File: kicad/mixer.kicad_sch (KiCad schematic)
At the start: 1 part

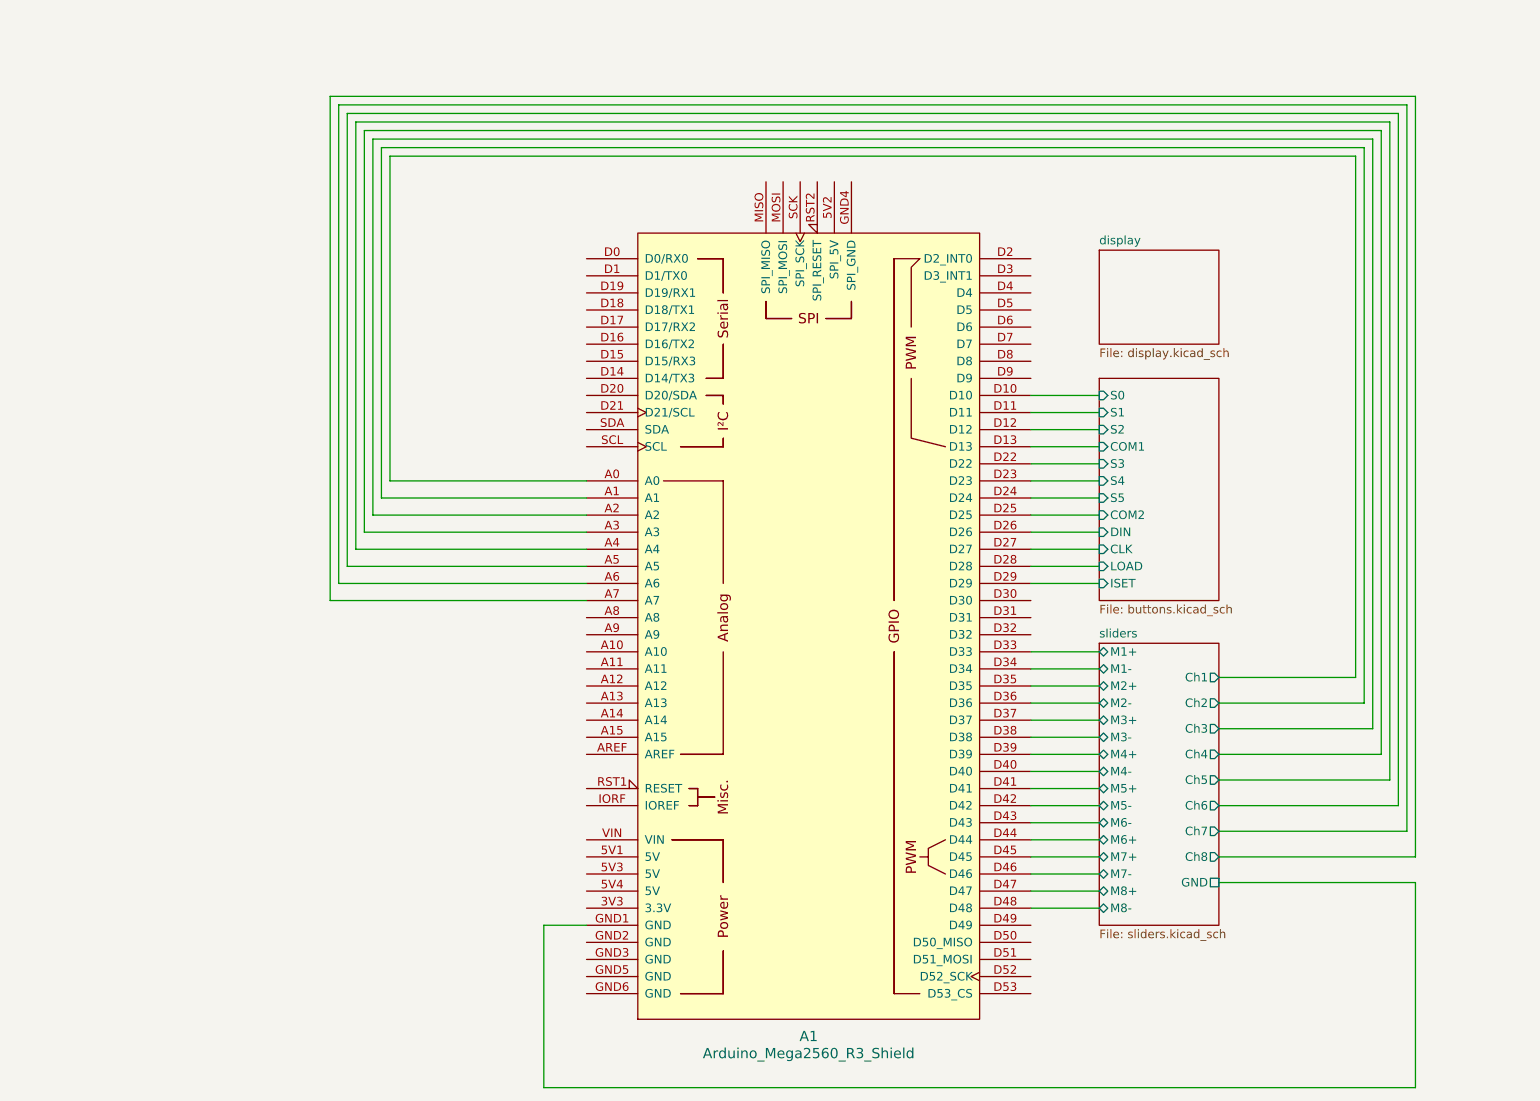
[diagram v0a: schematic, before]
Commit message: gain, meter and display sheets
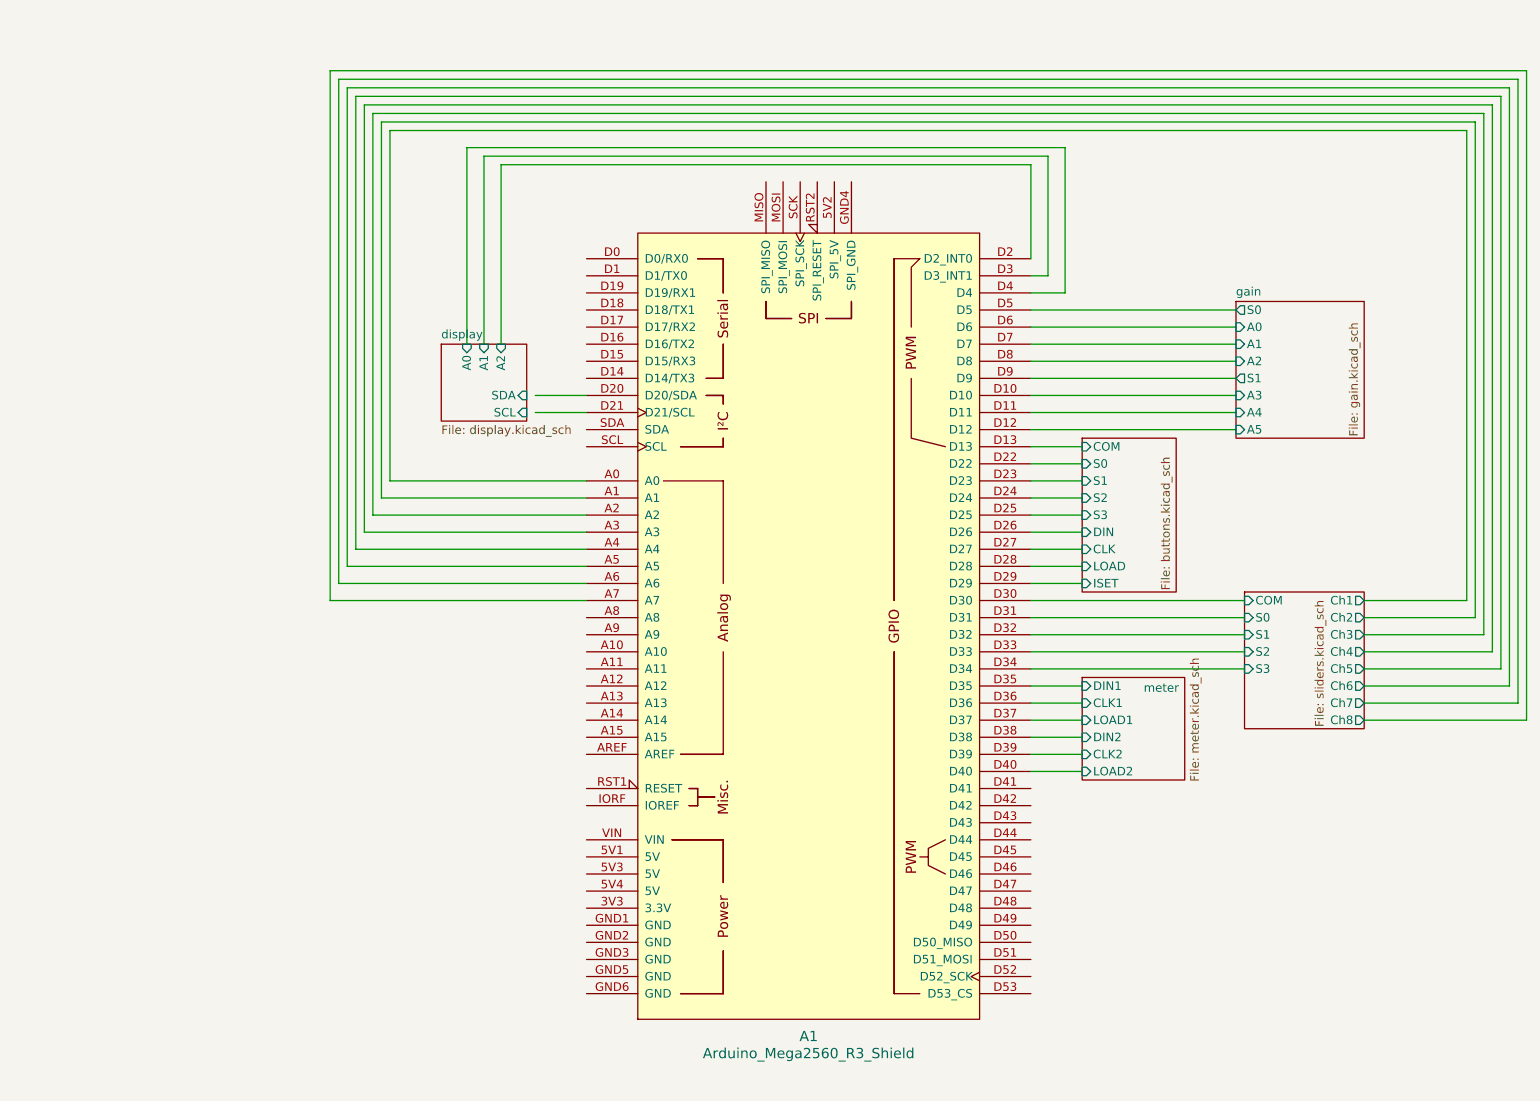
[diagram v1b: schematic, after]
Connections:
- net buttons/COM2 is gone; now on net buttons/S3: A1.D25
- net buttons/S4 is gone; now on net buttons/S1: A1.D23
- net buttons/S5 is gone; now on net buttons/S2: A1.D24
- net buttons/S0: now also A1.D22; no longer A1.D10
- net buttons/S1: no longer A1.D11
- net buttons/S2: no longer A1.D12
- net buttons/S3: no longer A1.D22
- net display/A2: now reaches A1.D2 (D2_INT0)
- net display/A1: now reaches A1.D3 (D3_INT1)
- net sliders/COM: now reaches A1.D30
- net sliders/S0: now reaches A1.D31
- net sliders/S1: now reaches A1.D32
- net display/A0: now reaches A1.D4
- net gain/S0: now reaches A1.D5
- net gain/A0: now reaches A1.D6
- net gain/A1: now reaches A1.D7
- net gain/A2: now reaches A1.D8
- net gain/S1: now reaches A1.D9
- net buttons/COM1 renamed buttons/COM
- net sliders/GND: no longer names the net of A1.GND1 (GND)
- net sliders/M1+ renamed sliders/S2
- net sliders/M1- renamed sliders/S3
- net sliders/M2+ renamed meter/DIN1
- net sliders/M2- renamed meter/CLK1
- net sliders/M3+ renamed meter/LOAD1
- net sliders/M3- renamed meter/DIN2
- net sliders/M4+ renamed meter/CLK2
- net sliders/M4- renamed meter/LOAD2
- net sliders/M5+: no longer names the net of A1.D41
- net sliders/M5-: no longer names the net of A1.D42
- net sliders/M6+: no longer names the net of A1.D44
- net sliders/M6-: no longer names the net of A1.D43
- net sliders/M7+: no longer names the net of A1.D45
- net sliders/M7-: no longer names the net of A1.D46
- net sliders/M8+: no longer names the net of A1.D47
- net sliders/M8-: no longer names the net of A1.D48
- new net gain/A3: A1.D10
- new net gain/A4: A1.D11
- new net gain/A5: A1.D12
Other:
- added sheet gain (gain.kicad_sch)
- added sheet meter (meter.kicad_sch)
- sheet buttons ports: added COM; removed COM1, COM2, S4, S5
- sheet display ports: added A0, A1, A2, SCL, SDA; removed none
- sheet sliders ports: added COM, S0, S1, S2, S3; removed GND, M1+, M1-, M2+, M2-, M3+, M3-, M4+, M4-, M5+, M5-, M6+, M6-, M7+, M7-, M8+, M8-

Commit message: kicad updates
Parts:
- added 1, 11, 111: HEADER-10, Connector_PinHeader_2.54mm:PinHeader_1x10_P2.54mm_Horizontal, symbol mixer:HEADER-10
- A1: footprint PCM_arduino-library:Arduino_Mega2560_R3_Shield -> arduino-library:Arduino_Mega2560_R3_Shield
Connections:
- net buttons/CLK: now also 1.6; no longer A1.D27
- net buttons/COM: now also 11.10; no longer A1.D13
- net buttons/DIN: now also 1.5; no longer A1.D26
- net buttons/LOAD: now also 1.7; no longer A1.D28
- net buttons/S0: now also 1.1; no longer A1.D22
- net buttons/S1: now also 1.2; no longer A1.D23
- net buttons/S2: now also 1.3; no longer A1.D24
- net buttons/S3: now also 1.4; no longer A1.D25
- net display/A0: now also 11.2; no longer A1.D4
- net display/A1: now also 11.3; no longer A1.D3 (D3_INT1)
- net display/A2: now also 11.4; no longer A1.D2 (D2_INT0)
- net display/SCL: now also 11.1
- net display/SDA: now also 111.1
- net gain/S0: now also 11.6; no longer A1.D5
- net gain/S1: now also 11.7; no longer A1.D9
- net buttons/ISET: no longer names the net of A1.D29
- net gain/A0: no longer names the net of A1.D6
- net gain/A1: no longer names the net of A1.D7
- net gain/A2: no longer names the net of A1.D8
- net gain/A3: no longer names the net of A1.D10
- net gain/A4: no longer names the net of A1.D11
- net gain/A5: no longer names the net of A1.D12
- net meter/CLK1: no longer names the net of A1.D36
- net meter/CLK2: no longer names the net of A1.D39
- net meter/DIN1: no longer names the net of A1.D35
- net meter/DIN2: no longer names the net of A1.D38
- net meter/LOAD1: no longer names the net of A1.D37
- net meter/LOAD2: no longer names the net of A1.D40
- new net gain/COM: 11.5
- new net gain/S2: 11.8
- new net gain/S3: 11.9
- new net meter/CLK: 1.10
- new net meter/DIN: 1.8
- new net meter/LOAD: 1.9
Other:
- sheet buttons ports: added none; removed ISET
- sheet gain ports: added COM, S2, S3; removed A0, A1, A2, A3, A4, A5
- sheet meter ports: added CLK, DIN, LOAD; removed CLK1, CLK2, DIN1, DIN2, LOAD1, LOAD2

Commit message: pcb routing 2
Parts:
- 1, 11, 111: footprint Connector_PinHeader_2.54mm:PinHeader_1x10_P2.54mm_Horizontal -> (none)
- A1: footprint arduino-library:Arduino_Mega2560_R3_Shield -> PCM_arduino-library:Arduino_Mega2560_R3_Shield
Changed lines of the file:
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@@
 			)
 		)
-		(property "Footprint" "Connector_PinHeader_2.54mm:PinHeader_1x10_P2.54mm_Horizontal"
+		(property "Footprint" ""
 			(at 222.25 18.034 0)
 			(effects
@@
 			)
 		)
-		(property "Footprint" "Connector_PinHeader_2.54mm:PinHeader_1x10_P2.54mm_Horizontal"
+		(property "Footprint" ""
 			(at 222.25 43.434 0)
 			(effects
@@
 			)
 		)
-		(property "Footprint" "arduino-library:Arduino_Mega2560_R3_Shield"
+		(property "Footprint" "PCM_arduino-library:Arduino_Mega2560_R3_Shield"
 			(at 132.08 168.91 0)
 			(effects
@@
 			)
 		)
-		(property "Footprint" "Connector_PinHeader_2.54mm:PinHeader_1x10_P2.54mm_Horizontal"
+		(property "Footprint" ""
 			(at 196.596 78.74 0)
 			(effects

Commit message: esp idf testing
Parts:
- removed 1, 11, 111: HEADER-10, symbol mixer:HEADER-10
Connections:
- net sliders/COM: no longer A1.D30
- net sliders/S0: no longer A1.D31
- net sliders/S1: no longer A1.D32
- net sliders/S2: no longer A1.D33
- net sliders/S3: no longer A1.D34
- net channel/SCK: now reaches A1.SCL
- net channel/SDA: now reaches A1.SDA
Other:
- removed sheet buttons
- removed sheet gain
- removed sheet meter
- added sheet channel (channel.kicad_sch)
- moved on the sheet: A1
